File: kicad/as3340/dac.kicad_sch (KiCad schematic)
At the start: 27 parts, among them U12 TL074, U13 LM4040AIM3-2.5, U14 AD5328

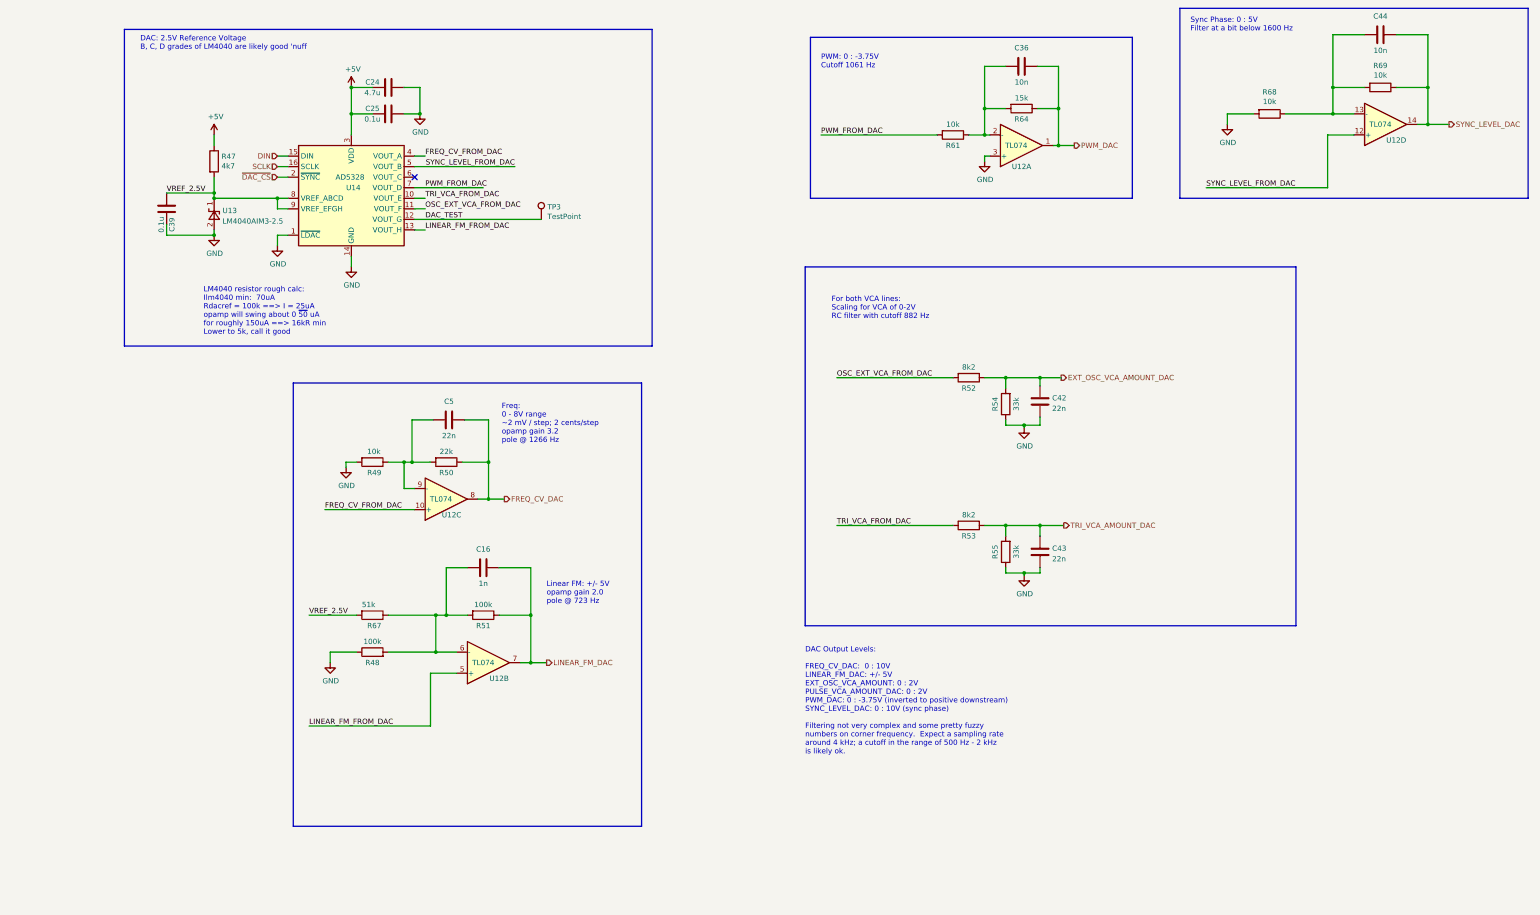
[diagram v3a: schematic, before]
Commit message: working through 3340 changes.  Added sync circuits, DAC scaling changes, 16:1 multiplexor
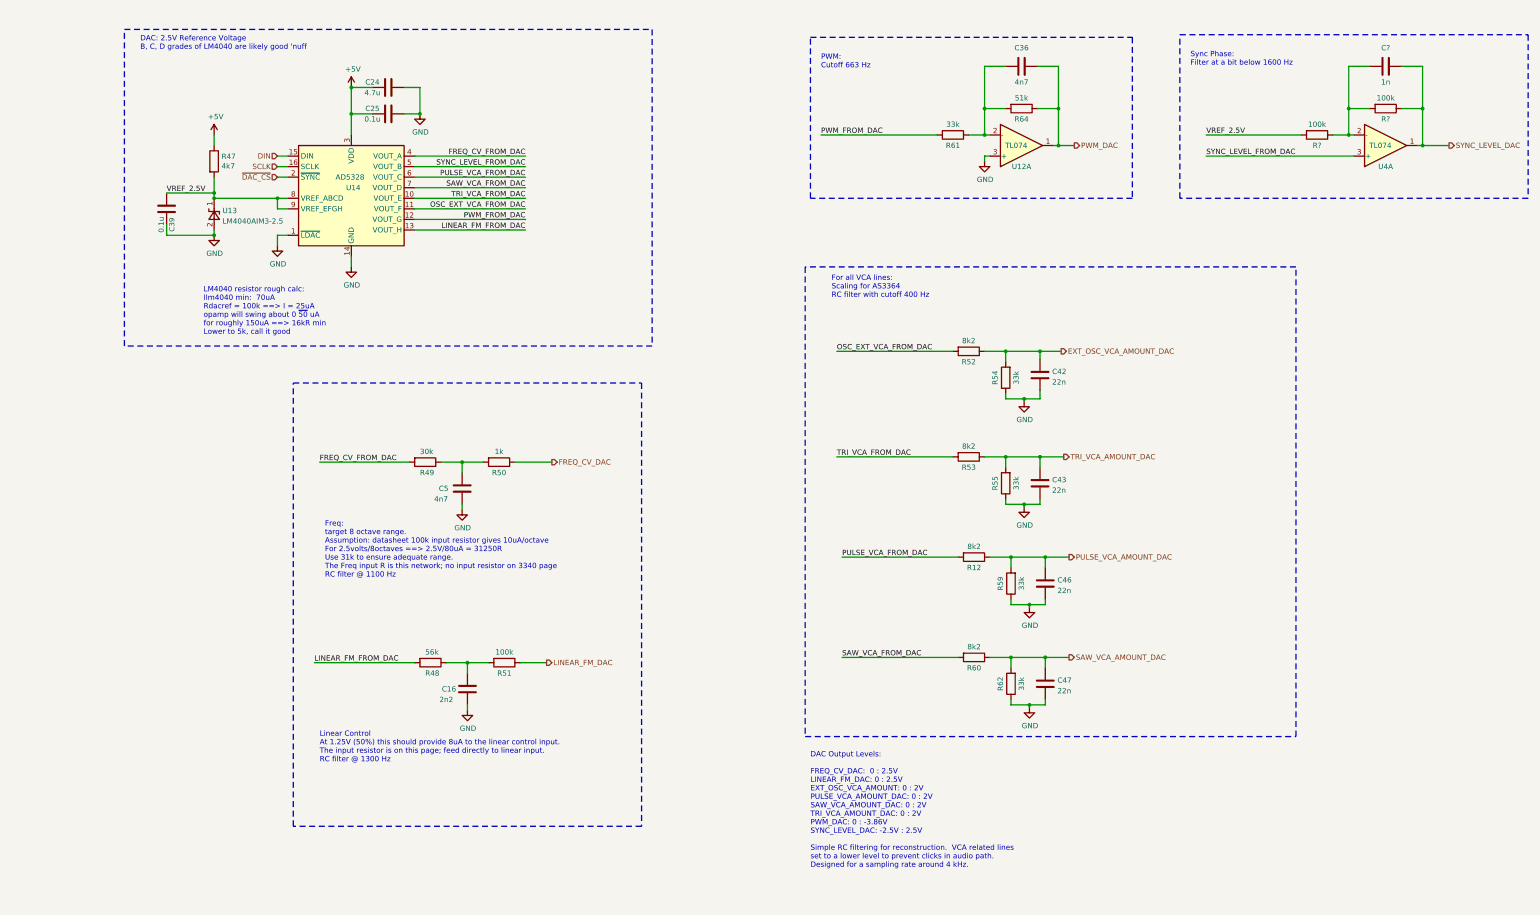
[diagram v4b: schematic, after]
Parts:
- removed C44: 10n, Capacitor_SMD:C_0603_1608Metric, symbol Device:C
- removed R67: 51k, Resistor_SMD:R_0603_1608Metric, symbol Device:R
- removed R68, R69: 10k, Resistor_SMD:R_0603_1608Metric, symbol Device:R
- removed TP3: TestPoint, TestPoint:TestPoint_Pad_2.0x2.0mm, symbol Connector:TestPoint
- removed unit 4 of U12
- removed unit 3 of U12
- removed unit 2 of U12
- added C46, C47: 22n, Capacitor_SMD:C_0603_1608Metric, symbol Device:C
- added C?: 1n, Capacitor_SMD:C_0603_1608Metric, symbol Device:C
- added R12, R60: 8k2, Resistor_SMD:R_0603_1608Metric, symbol Device:R
- added R59, R62: 33k, Resistor_SMD:R_0603_1608Metric, symbol Device:R
- added R? (x2): 100k, Resistor_SMD:R_0603_1608Metric, symbol Device:R
- added U4: TL074, Package_SO:SOIC-14_3.9x8.7mm_P1.27mm, symbol Amplifier_Operational:TL074
- C16: value 1n -> 2n2; LCSC Part C1588 -> (none)
- C36: value 10n -> 4n7; LCSC Part C57112 -> (none)
- C5: value 22n -> 4n7; LCSC Part C21122 -> (none)
- R48: value 100k -> 56k; LCSC Part C25803 -> (none)
- R49: value 10k -> 30k; LCSC Part C25804 -> (none)
- R50: value 22k -> 1k; LCSC Part C31850 -> (none)
- R51: LCSC Part C25803 -> (none)
- R61: value 10k -> 33k; LCSC Part C25804 -> (none)
- R64: value 15k -> 51k; LCSC Part C22809 -> (none)
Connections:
- net DAC_TEST is gone; now on net PWM_FROM_DAC: U14.12 (VOUT_G)
- net FREQ_CV_DAC: no longer C5.2
- net FREQ_CV_FROM_DAC: now also R49.2
- net GND: now also C16.1, C5.1, C46.2, C47.2, R59.1, R62.1; no longer R48.1, R49.2
- net LINEAR_FM_DAC: no longer C16.2
- net LINEAR_FM_FROM_DAC: now also R48.2
- net PWM_FROM_DAC: no longer U14.7 (VOUT_D)
- net SYNC_LEVEL_DAC: now also C?.2, R?.1, U4.1
- net SYNC_LEVEL_FROM_DAC: now also U4.3 (+)
- net VREF_2.5V: now also R?.2
- net at R49.1, R50.2: now also C5.2; no longer C5.1
- net PULSE_VCA_FROM_DAC: now reaches U14.6 (VOUT_C)
- net PULSE_VCA_FROM_DAC: now also R12.2
- new net: C?.1, R?.1, R?.2, U4.2 (-)
- new net: C16.2, R48.1, R51.2
- new net PULSE_VCA_AMOUNT_DAC: C46.1, R12.1, R59.2
- new net SAW_VCA_AMOUNT_DAC: C47.1, R60.1, R62.2
- new net SAW_VCA_FROM_DAC: R60.2, U14.7 (VOUT_D)
- no-connect marks 1 -> 0
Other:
- note added: "DAC Output Levels: FREQ_CV_DAC: 0 : 2.5V LINEAR_FM_DAC: 0 : 2.5V EXT_OSC_VCA_AMOUNT: 0 : 2V PULSE_VCA_AMOUNT_DAC: 0 : 2V SAW_VCA_AMOUNT_DAC: 0 : 2V TRI_VCA_AMOUNT_DAC: 0 : 2V PWM_DAC: 0 : -3.86V SYNC_LEVEL_DAC: -2.5V : 2.5V Simple RC filtering for reconstruction. VCA related lines set to a lower level to prevent clicks in audio path. Designed for a sampling rate around 4 kHz."
- note added: "For all VCA lines: Scaling for AS3364 RC filter with cutoff 400 Hz"
- note added: "Freq: target 8 octave range. Assumption: datasheet 100k input resistor gives 10uA/octave For 2.5volts/8octaves ==> 2.5V/80uA = 31250R Use 31k to ensure adequate range. The Freq input R is this network; no input resistor on 3340 page RC filter @ 1100 Hz"
- note added: "Linear Control At 1.25V (50%) this should provide 8uA to the linear control input. The input resistor is on this page; feed directly to linear input. RC filter @ 1300 Hz"
- note added: "PWM: Cutoff 663 Hz"
- note added: "Sync Phase: Filter at a bit below 1600 Hz"
- note removed: "DAC Output Levels: FREQ_CV_DAC: 0 : 10V LINEAR_FM_DAC: +/- 5V EXT_OSC_VCA_AMOUNT: 0 : 2V PULSE_VCA_AMOUNT_DAC: 0 : 2V PWM_DAC: 0 : -3.75V (inverted to positive downstream) SYNC_LEVEL_DAC: 0 : 10V (sync phase) Filtering not very complex and some pretty fuzzy numbers on corner frequency. Expect a sampling rate around 4 kHz; a cutoff in the range of 500 Hz - 2 kHz is likely ok."
- note removed: "For both VCA lines: Scaling for VCA of 0-2V RC filter with cutoff 882 Hz"
- note removed: "Freq: 0 - 8V range ~2 mV / step; 2 cents/step opamp gain 3.2 pole @ 1266 Hz"
- note removed: "Linear FM: +/- 5V opamp gain 2.0 pole @ 723 Hz"
- note removed: "PWM: 0 : -3.75V Cutoff 1061 Hz"
- note removed: "Sync Phase: 0 : 5V Filter at a bit below 1600 Hz"
- moved on the sheet: C42, C43, C5, R49, R50, R52, R53, R54, R55

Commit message: schematic capture z3340 about done; starting placement
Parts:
- removed C39: 0.1u, Capacitor_SMD:C_0603_1608Metric, symbol Device:C
- removed C5: 4n7, Capacitor_SMD:C_0603_1608Metric, symbol Device:C
- removed R47: 4k7, Resistor_SMD:R_1206_3216Metric, symbol Device:R
- removed R48: 56k, Resistor_SMD:R_0603_1608Metric, symbol Device:R
- removed R49: 30k, Resistor_SMD:R_0603_1608Metric, symbol Device:R
- removed U12, U4: TL074, Package_SO:SOIC-14_3.9x8.7mm_P1.27mm, symbol Amplifier_Operational:TL074
- removed U13: LM4040AIM3-2.5, Package_TO_SOT_SMD:SOT-23, symbol Reference_Voltage:LM4040DBZ-2.5
- added C18, C8: 0.1u, Capacitor_SMD:C_0603_1608Metric, symbol Device:C
- added U5: TL074, Package_SO:TSSOP-14_4.4x5mm_P0.65mm, symbol Amplifier_Operational:TL074
- C16: value 2n2 -> 22n; LCSC Part (none) -> C2761748
- R51: value 100k -> 5k6; LCSC Part (none) -> C23189
- gave numbers to parts that had none: 3
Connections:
- net FREQ_CV_DAC: now also C8.2
- net FREQ_CV_FROM_DAC: now also R50.2
- net GND: now also C18.1, C8.1, U5.3 (+)
- net LINEAR_FM_DAC: now also C16.2
- net LINEAR_FM_FROM_DAC: now also R51.2
- net PWM_DAC: now also U5.1
- net SYNC_LEVEL_DAC: now also U5.7
- net SYNC_LEVEL_FROM_DAC: now also U5.6 (-)
- net at C36.1, R61.1, R64.2: now also U5.2 (-)
- net at C3.1, R38.1, R39.2: now also U5.5 (+)
- net VREF_2.5V renamed VREF_2.5
- net VREF_2.5: now also C18.2
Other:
- note added: "DAC Output Levels: FREQ_CV_DAC: 0 : 2.5V LINEAR_FM_DAC: 0 : 2.5V EXT_OSC_VCA_AMOUNT: 0 : 2V PULSE_VCA_AMOUNT_DAC: 0 : 2V SAW_VCA_AMOUNT_DAC: 0 : 2V TRI_VCA_AMOUNT_DAC: 0 : 2V PWM_DAC: 0 : -3.86V SYNC_LEVEL_DAC: -2.5V : 2.5V Simple RC filtering for reconstruction. VCA related lines set to a lower level to prevent clicks in audio path. Designed for a sampling rate around 4 kHz. Sheet Vref Load: 45k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"
- note added: "DAC: 2.5V Reference Voltage Vref load: 45k"
- note added: "Freq: target 8 octave range. Assumption: datasheet 100k input resistor gives 10uA/octave For 2.5volts/8octaves ==> 2.5V/80uA = 31250R Use 31k to ensure adequate range. The Freq input R is this network; no input resistor on 3340 page RC filter @ 1600 Hz"
- note added: "Local cap for Vref"
- note removed: "DAC Output Levels: FREQ_CV_DAC: 0 : 2.5V LINEAR_FM_DAC: 0 : 2.5V EXT_OSC_VCA_AMOUNT: 0 : 2V PULSE_VCA_AMOUNT_DAC: 0 : 2V SAW_VCA_AMOUNT_DAC: 0 : 2V TRI_VCA_AMOUNT_DAC: 0 : 2V PWM_DAC: 0 : -3.86V SYNC_LEVEL_DAC: -2.5V : 2.5V Simple RC filtering for reconstruction. VCA related lines set to a lower level to prevent clicks in audio path. Designed for a sampling rate around 4 kHz."
- note removed: "DAC: 2.5V Reference Voltage B, C, D grades of LM4040 are likely good 'nuff"
- note removed: "Freq: target 8 octave range. Assumption: datasheet 100k input resistor gives 10uA/octave For 2.5volts/8octaves ==> 2.5V/80uA = 31250R Use 31k to ensure adequate range. The Freq input R is this network; no input resistor on 3340 page RC filter @ 1100 Hz"
- note removed: "LM4040 resistor rough calc: Ilm4040 min: 70uA Rdacref = 100k ==> I = 25uA opamp will swing about 0 ~{50} uA for roughly 150uA ==> 16kR min Lower to 5k, call it good"
- moved on the sheet: R50, R51

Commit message: z3340 placement getting close to good
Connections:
- net FREQ_CV_FROM_DAC: now also U14.5 (VOUT_B); no longer U14.4 (VOUT_A)
- net GND: now also U5.5 (+); no longer U5.3 (+)
- net PWM_DAC: now also U5.7; no longer U5.1
- net SYNC_LEVEL_DAC: now also U5.1; no longer U5.7
- net SYNC_LEVEL_FROM_DAC: now also U14.4 (VOUT_A), U5.3 (+); no longer U14.5 (VOUT_B), U5.6 (-)
- net at C36.1, R61.1, R64.2: now also U5.6 (-); no longer U5.2 (-)
- net at C3.1, R38.1, R39.2: now also U5.2 (-); no longer U5.5 (+)
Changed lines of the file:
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@@
     (effects (font (size 1.27 1.27)) (justify left bottom))
   )
-  (label "FREQ_CV_FROM_DAC" (at 142.24 63.5 180) (fields_autoplaced)
+  (label "FREQ_CV_FROM_DAC" (at 142.24 66.04 180) (fields_autoplaced)
     (effects (font (size 1.27 1.27)) (justify right bottom))
   )
-  (label "SYNC_LEVEL_FROM_DAC" (at 142.24 66.04 180) (fields_autoplaced)
+  (label "SYNC_LEVEL_FROM_DAC" (at 142.24 63.5 180) (fields_autoplaced)
     (effects (font (size 1.27 1.27)) (justify right bottom))
   )
@@
     )
   )
-  (symbol (lib_id "Amplifier_Operational:TL074") (at 349.25 60.96 0) (unit 2)
-    (in_bom yes) (on_board yes) (dnp no)
-    (property "Reference" "U5" (at 351.155 64.77 0)
+  (symbol (lib_id "Amplifier_Operational:TL074") (at 349.25 60.96 0) (mirror x) (unit 1)
+    (in_bom yes) (on_board yes) (dnp no)
+    (property "Reference" "U5" (at 353.06 64.77 0)
       (effects (font (size 1.27 1.27)))
     )
@@
       (effects (font (size 1.27 1.27)))
     )
-    (property "Footprint" "Package_SO:TSSOP-14_4.4x5mm_P0.65mm" (at 347.98 58.42 0)
-      (effects (font (size 1.27 1.27)) hide)
-    )
-    (property "Datasheet" "http://www.ti.com/lit/ds/symlink/tl071.pdf" (at 350.52 55.88 0)
+    (property "Footprint" "Package_SO:TSSOP-14_4.4x5mm_P0.65mm" (at 347.98 63.5 0)
+      (effects (font (size 1.27 1.27)) hide)
+    )
+    (property "Datasheet" "http://www.ti.com/lit/ds/symlink/tl071.pdf" (at 350.52 66.04 0)
       (effects (font (size 1.27 1.27)) hide)
     )
@@
       (project "as3340"
         (path "/7079bdb0-a00e-4bac-b257-cbcf2c91bbd6/00000000-0000-0000-0000-000061ff2290"
-          (reference "U5") (unit 2)
+          (reference "U5") (unit 1)
         )
       )
@@
     )
   )
-  (symbol (lib_id "Amplifier_Operational:TL074") (at 261.62 60.96 0) (mirror x) (unit 1)
+  (symbol (lib_id "Amplifier_Operational:TL074") (at 261.62 60.96 0) (mirror x) (unit 2)
     (in_bom yes) (on_board yes) (dnp no)
     (property "Reference" "U5" (at 262.89 65.405 0)
@@
       (project "as3340"
         (path "/7079bdb0-a00e-4bac-b257-cbcf2c91bbd6/00000000-0000-0000-0000-000061ff2290"
-          (reference "U5") (unit 1)
-        )
-      )
+          (reference "U5") (unit 2)
+        )
+      )

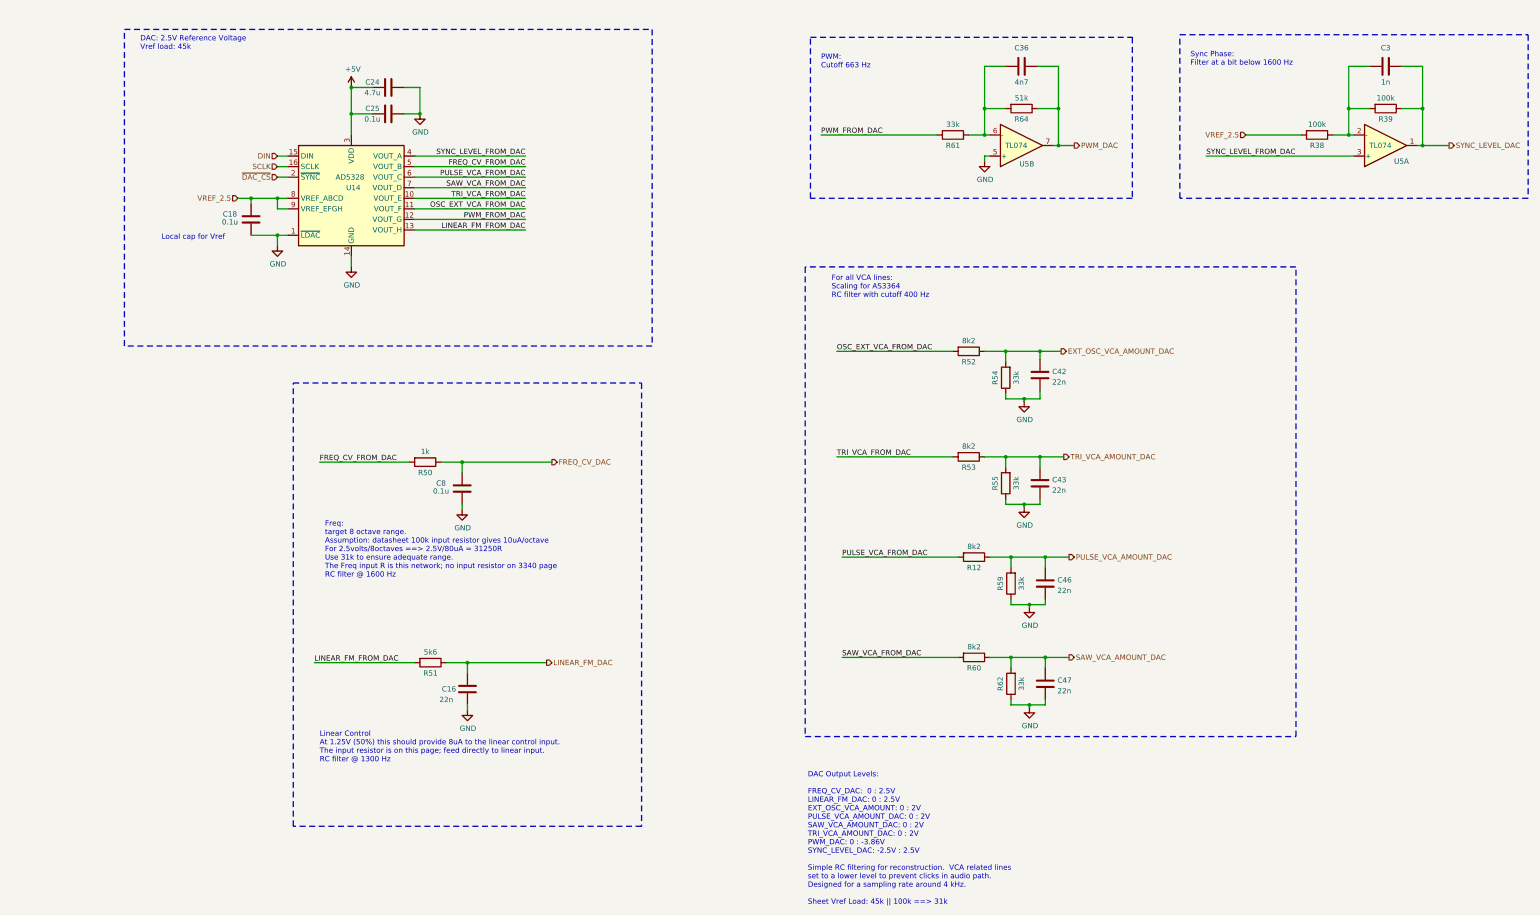
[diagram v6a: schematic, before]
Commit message: routed.  not very clean, but routed.
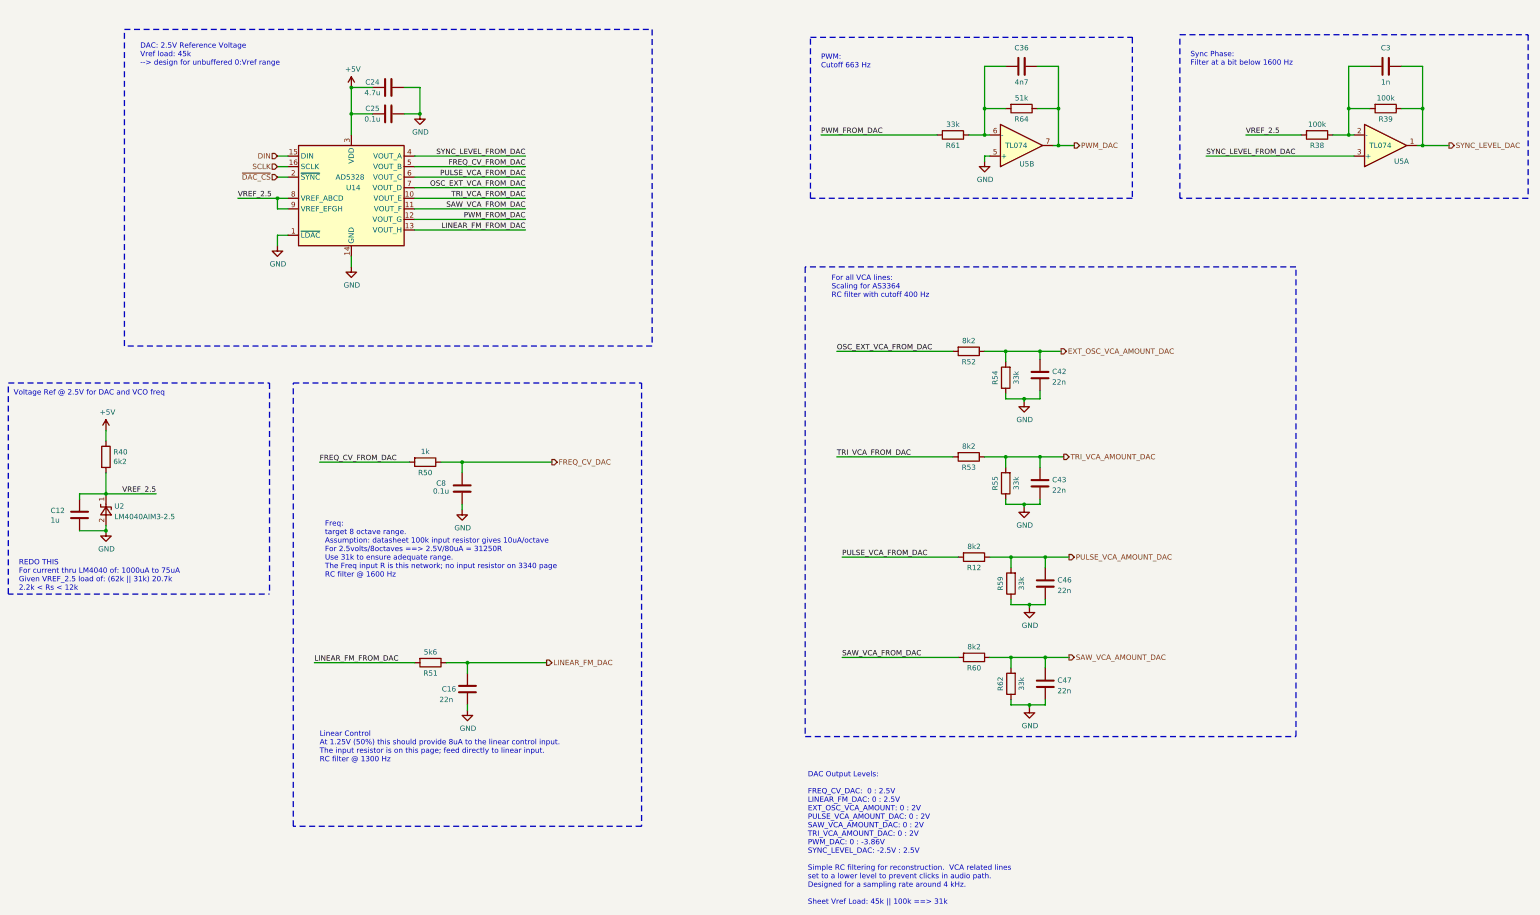
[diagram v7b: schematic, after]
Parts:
- removed C18: 0.1u, Capacitor_SMD:C_0603_1608Metric, symbol Device:C
- added C12: 1u, Capacitor_SMD:C_0603_1608Metric, symbol Device:C
- added R40: 6k2, Resistor_SMD:R_1206_3216Metric, symbol Device:R
- added U2: LM4040AIM3-2.5, Package_TO_SOT_SMD:SOT-23, symbol Reference_Voltage:LM4040DBZ-2.5
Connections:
- net +5V: now also R40.1
- net GND: now also C12.2, U2.2 (A)
- net OSC_EXT_VCA_FROM_DAC: now also U14.7 (VOUT_D); no longer U14.11 (VOUT_F)
- net SAW_VCA_FROM_DAC: now also U14.11 (VOUT_F); no longer U14.7 (VOUT_D)
- net VREF_2.5: now also C12.1, R40.2, U2.1 (K)
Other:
- note added: "DAC: 2.5V Reference Voltage Vref load: 45k --> design for unbuffered 0:Vref range"
- note added: "REDO THIS For current thru LM4040 of: 1000uA to 75uA Given VREF_2.5 load of: (62k || 31k) 20.7k 2.2k < Rs < 12k"
- note added: "Voltage Ref @ 2.5V for DAC and VCO freq"
- note removed: "DAC: 2.5V Reference Voltage Vref load: 45k"
- note removed: "Local cap for Vref"
